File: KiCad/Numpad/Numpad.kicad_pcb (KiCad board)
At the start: 2 copper layers, 81 x 95.3 mm, 35 parts, among them SW1 SW_SPDT_312, U1 Promicro_NRF52840

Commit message: changed to the kicad files
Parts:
- moved BT1 2.38 mm to (121.4, 57.1)
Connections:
- BT1 pad : (no net) -> Net-(BT1-+)
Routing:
- net Row_1: track 68.3 -> 140.5 mm
- net Net-(BT1-+): track 8.68 -> 32.0 mm
- net B-: track 53.4 -> 74.3 mm
- net Row_4: track 178.4 -> 192.9 mm
- net Row_2: track 144.8 -> 157.9 mm
- net Row_3: track 162.2 -> 174.8 mm
- net Col_4: track 166.1 -> 169.6 mm
- net Col_3: track 154.4 -> 157.7 mm
- net Col_2: track 139.3 -> 142.1 mm
- net Col_1: track 128.4 -> 131.3 mm
- net B+: track 72.2 -> 74.6 mm

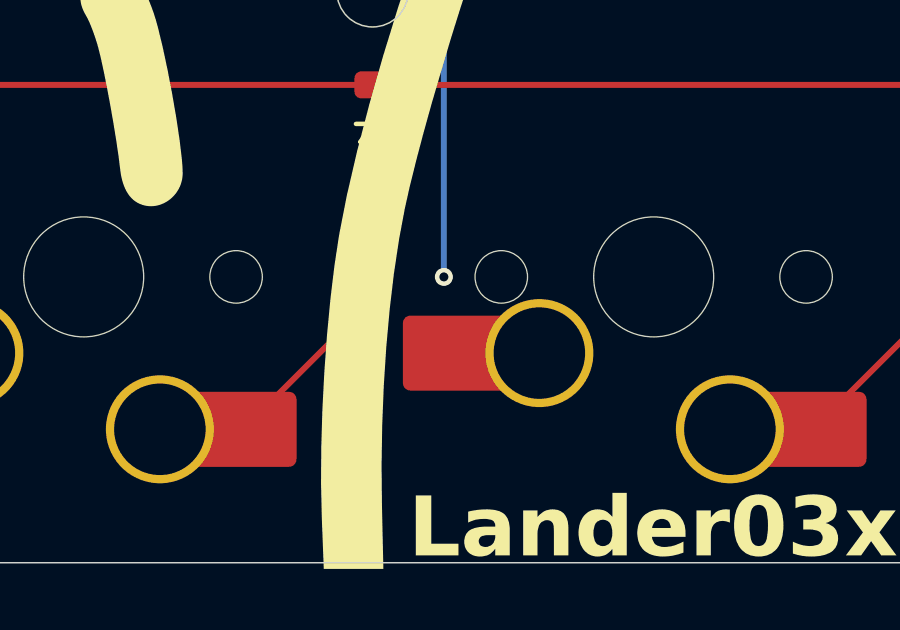
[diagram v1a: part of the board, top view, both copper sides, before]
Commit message: keymap rework
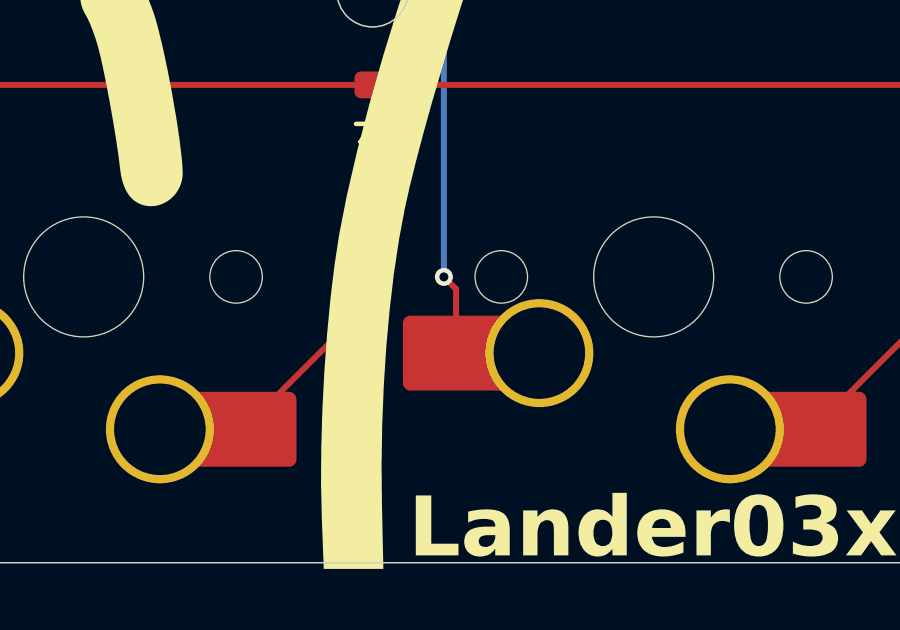
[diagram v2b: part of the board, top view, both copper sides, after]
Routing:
- net Col_4: track 169.6 -> 172.3 mm
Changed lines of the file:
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@@
+	)
+	(segment
+		(start 155.19 135.89)
+		(end 155.19 133.75875)
+		(width 0.2)
+		(layer "F.Cu")
+		(net 24)
+	)
+	(segment
+		(start 155.19 133.75875)
+		(end 154.78125 133.35)
+		(width 0.2)
+		(layer "F.Cu")
+		(net 24)
 	)
 	(segment
